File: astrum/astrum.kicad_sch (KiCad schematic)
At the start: 17 parts, among them J1 USB_C_Receptacle_USB2.0_16P, J2 Micro_SD_Card, U1 STM32H523CEUx, U3 USBLC6-2SC6, U4 W25Q32JVSS, Y1 25 mHz

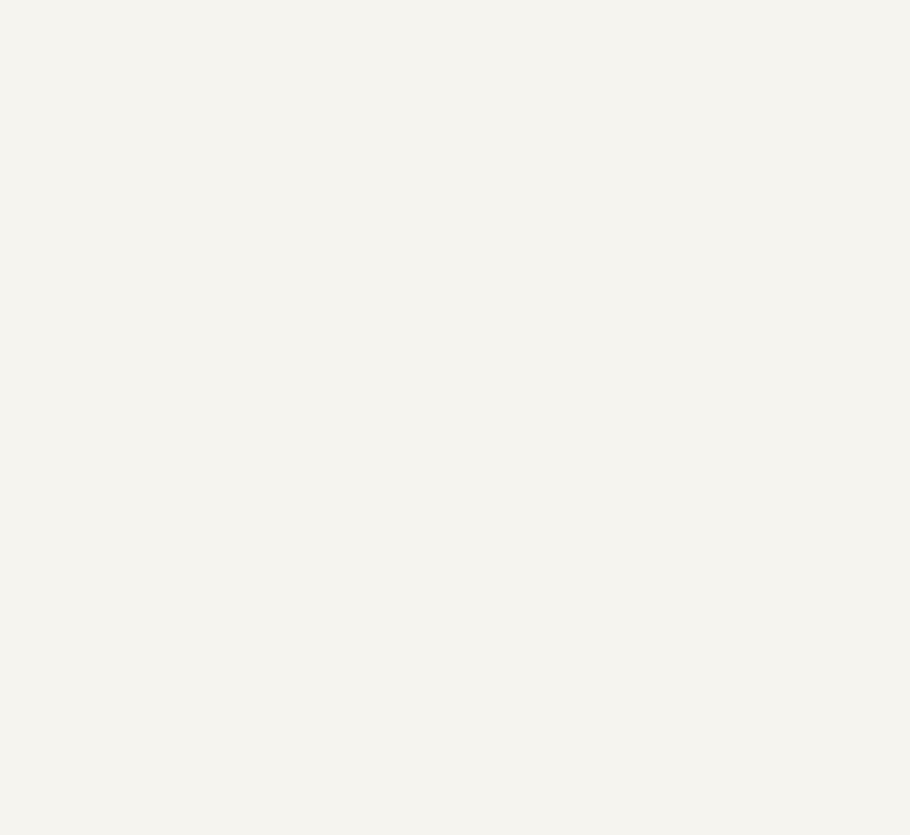
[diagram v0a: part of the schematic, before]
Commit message: add drv8871 drivers to the board
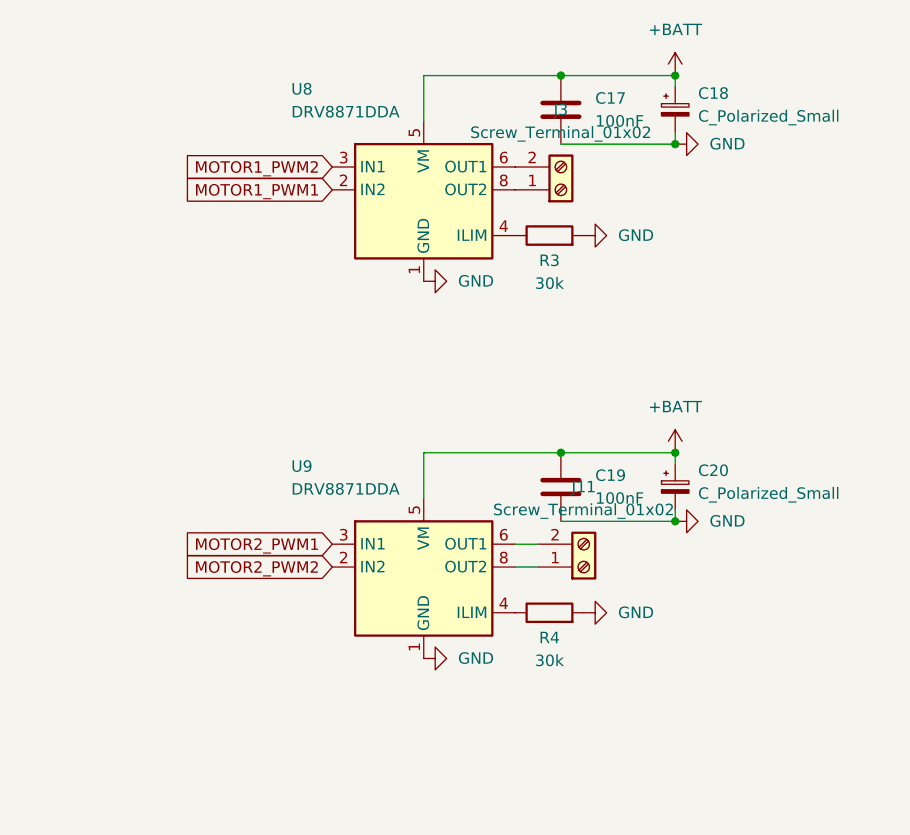
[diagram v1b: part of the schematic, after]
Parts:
- added C17, C19: 100nF, A_HDJ_Library:C_0603_1608Metric, symbol Device:C
- added C18, C20: C_Polarized_Small, Capacitor_SMD:CP_Elec_3x5.3, symbol Device:C_Polarized_Small
- added J11, J3: Screw_Terminal_01x02, TerminalBlock:TerminalBlock_bornier-2_P5.08mm, symbol Connector:Screw_Terminal_01x02
- added R3, R4: 30k, Resistor_SMD:R_0603_1608Metric, symbol Device:R
- added U8, U9: DRV8871DDA, Package_SO:Texas_HTSOP-8-1EP_3.9x4.9mm_P1.27mm_EP2.95x4.9mm_Mask2.4x3.1mm_ThermalVias, symbol Driver_Motor:DRV8871DDA
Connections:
- net GND: now also C17.2, C18.2, C19.2, C20.2, R3.2, R4.2, U8.1 (GND), U8.7 (GND), U8.9 (GND), U9.1 (GND), U9.7 (GND), U9.9 (GND)
- net MOTOR1_PWM1: now also U8.2 (IN2)
- net MOTOR1_PWM2: now also U8.3 (IN1)
- net MOTOR2_PWM1: now also U9.3 (IN1)
- net MOTOR2_PWM2: now also U9.2 (IN2)
- new net: R4.1, U9.4 (ILIM)
- new net: J11.2 (Pin_2), U9.6 (OUT1)
- new net: J11.1 (Pin_1), U9.8 (OUT2)
- new net: R3.1, U8.4 (ILIM)
- new net: J3.2 (Pin_2), U8.6 (OUT1)
- new net: J3.1 (Pin_1), U8.8 (OUT2)
- new net +BATT: C17.1, C18.1, C19.1, C20.1, U8.5 (VM), U9.5 (VM)

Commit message: add imu schematics
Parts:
- added C10: 4.7uF, A_HDJ_Library:C_0603_1608Metric, symbol Device:C
- added C12, C13, C9: 1uF, A_HDJ_Library:C_0603_1608Metric, symbol Device:C
- added C14, C15, C16: 100nF, A_HDJ_Library:C_0603_1608Metric, symbol Device:C
- added D3: NSR0530HT3G, Diode_SMD:D_SOD-323, symbol Device:D_Schottky
- added R5, R7: YC164-JR-0710KL, YC164-JR-0710KL:RESCAXE80P320X160X70-8N, symbol YC164-JR-0710KL:YC164-JR-0710KL
- added U10, U7: BSS138DW-7-F, BSS138DW:SOT363_DIO, symbol 2025-10-04_02-12-38:BSS138DW-7-F
- added U2: LDL212PV33R, LDL212PV33R:SON50P200X200X80-7N, symbol LDL212PV33R:LDL212PV33R
- added U5: ICM-20948, Sensor_Motion:InvenSense_QFN-24_3x3mm_P0.4mm, symbol Sensor_Motion:ICM-20948
- added U6: MIC5317-1.8xM5, Package_TO_SOT_SMD:SOT-23-5, symbol Regulator_Linear:MIC5317-1.8xM5
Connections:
- net +5V: now also D3.2 (A)
- net +BATT: now also C9.1, D3.1 (K), U2.4 (VIN), U2.6 (EN)
- net GND: now also C10.2, C12.2, C13.2, C14.2, C15.2, C16.2, C9.2, U2.1 (GND), U2.7 (GND__1), U5.18 (GND), U5.20 (GND), U6.2 (GND)
- net IMU_INT: now also R5.2, U10.3 (D2)
- net IMU_SCL: now also R7.2, U7.3 (D2)
- net IMU_SDA: now also R7.3, U7.6 (D1)
- net VDD: now also C10.1, C12.1, R5.6, R5.7, R7.6, R7.7, U2.2 (SENSE), U2.3 (VOUT), U6.1 (VIN), U6.3 (EN)
- new net: C14.1, U5.10 (REGOUT)
- new net +1V8: C13.1, C15.1, C16.1, R5.5, R5.8, R7.5, R7.8, U10.2 (G1), U10.5 (G2), U5.13 (VDD), U5.22 (~{CS}), U5.8 (VDDIO), U6.5 (VOUT), U7.2 (G1), U7.5 (G2)
- new net FSYNC_1V8: R5.1, U10.1 (S1), U5.11 (FSYNC)
- new net IMU_FSYNC: R5.3, U10.6 (D1)
- new net INT_1V8: R5.4, U10.4 (S2), U5.12 (INT1)
- new net SCL_1V8: R7.4, U5.23 (SCL/SCLK), U7.4 (S2)
- new net SDA_1V8: R7.1, U5.24 (SDA/SDI), U7.1 (S1)
- no-connect marks 4 -> 6
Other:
- moved on the sheet: C17, C18, C19, C20, J11, J3, R3, R4, U8, U9

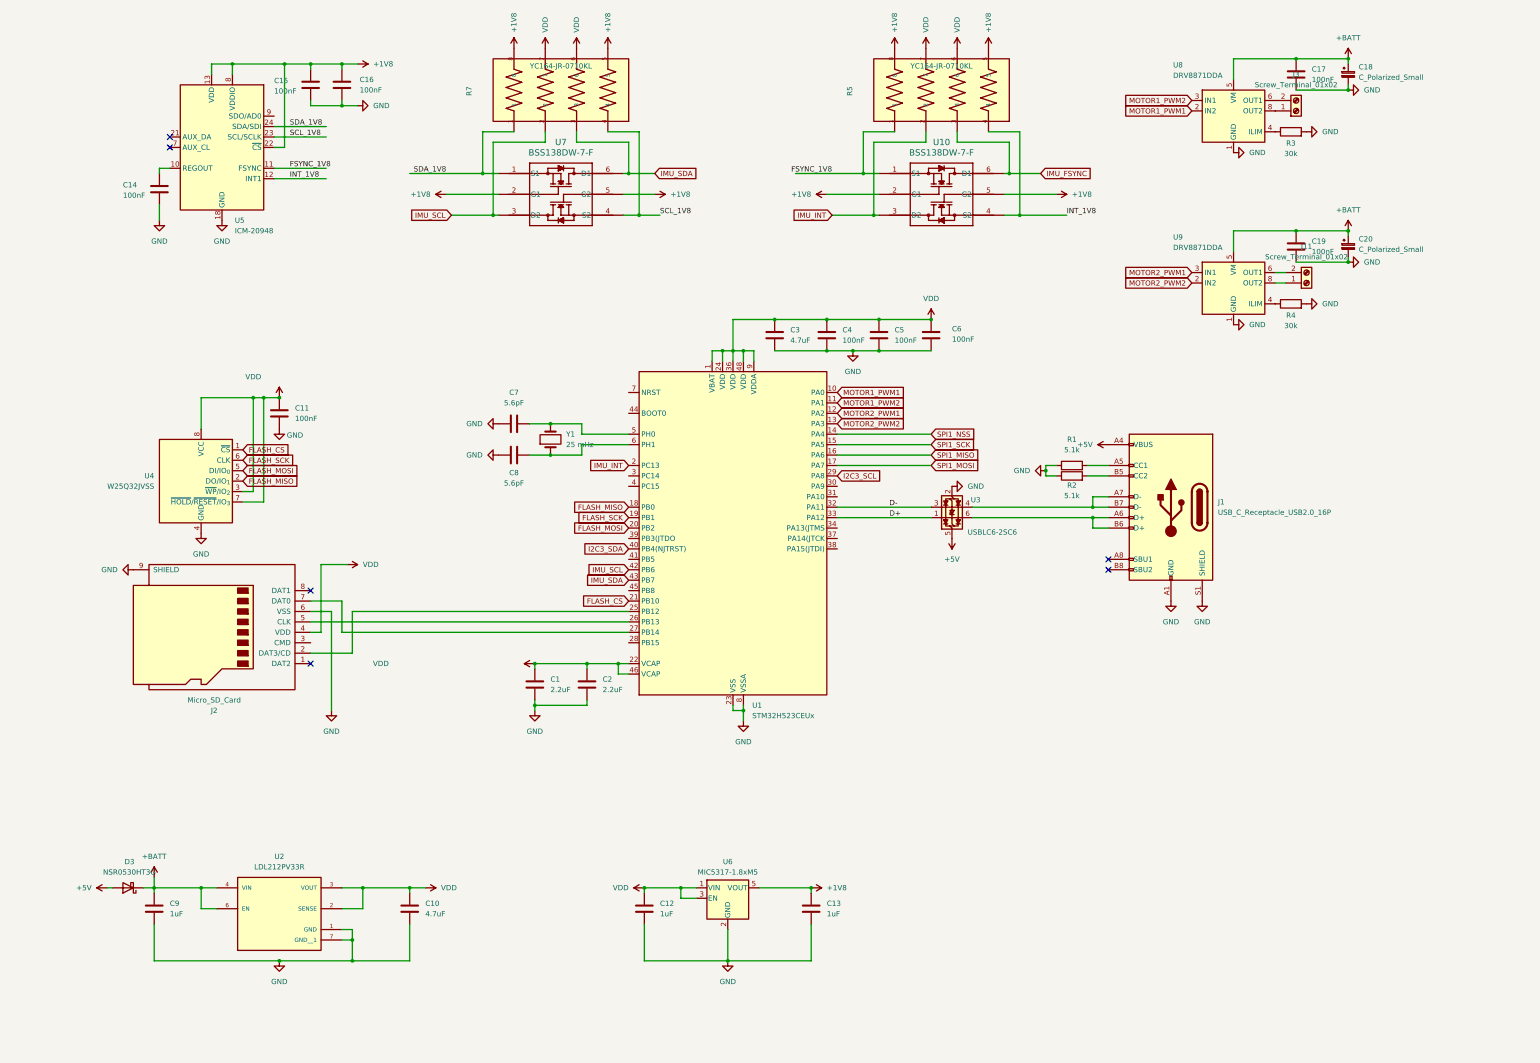
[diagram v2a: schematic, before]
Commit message: add the drv routing and header pins + power supply
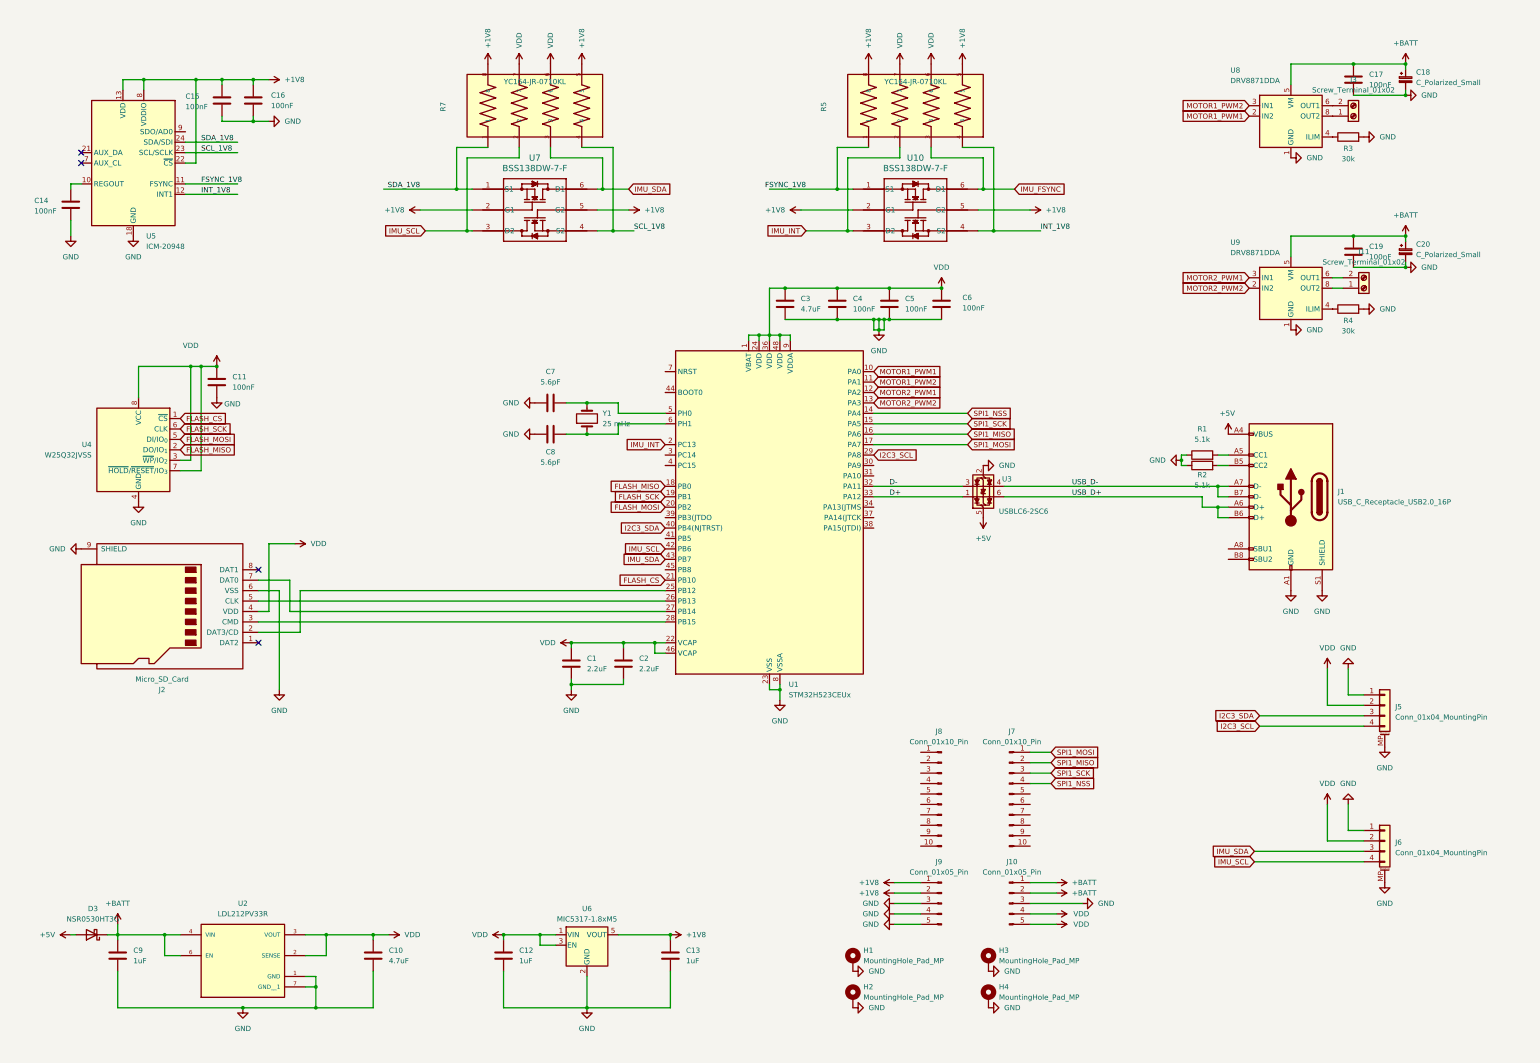
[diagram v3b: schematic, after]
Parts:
- added H1, H2, H3, H4: MountingHole_Pad_MP, MountingHole:MountingHole_2.2mm_M2_ISO7380_Pad, symbol Mechanical:MountingHole_Pad_MP
- added J10, J9: Conn_01x05_Pin, Connector_PinHeader_2.54mm:PinHeader_1x05_P2.54mm_Vertical, symbol Connector:Conn_01x05_Pin
- added J5, J6: Conn_01x04_MountingPin, Connector_JST:JST_SH_SM04B-SRSS-TB_1x04-1MP_P1.00mm_Horizontal, symbol Connector_Generic_MountingPin:Conn_01x04_MountingPin
- added J7, J8: Conn_01x10_Pin, Connector_PinHeader_2.54mm:PinHeader_1x10_P2.54mm_Vertical, symbol Connector:Conn_01x10_Pin
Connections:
- net +1V8: now also J9.1 (Pin_1), J9.2 (Pin_2)
- net +BATT: now also J10.1 (Pin_1), J10.2 (Pin_2)
- net GND: now also H1.MP, H2.MP, H3.MP, H4.MP, J10.3 (Pin_3), J5.1 (Pin_1), J5.MP (MountPin), J6.1 (Pin_1), J6.MP (MountPin), J9.3 (Pin_3), J9.4 (Pin_4), J9.5 (Pin_5)
- net I2C3_SCL: now also J5.4 (Pin_4)
- net I2C3_SDA: now also J5.3 (Pin_3)
- net IMU_SCL: now also J6.4 (Pin_4)
- net IMU_SDA: now also J6.3 (Pin_3)
- net SPI1_MISO: now also J7.2 (Pin_2)
- net SPI1_MOSI: now also J7.1 (Pin_1)
- net SPI1_NSS: now also J7.4 (Pin_4)
- net SPI1_SCK: now also J7.3 (Pin_3)
- net VDD: now also J10.4 (Pin_4), J10.5 (Pin_5), J5.2 (Pin_2), J6.2 (Pin_2)
- net at J2.3 (CMD): now also U1.28 (PB15)
- net USB_D+: now reaches J1.A6 (D+), J1.B6 (D+), U3.6 (I/O1)
- net USB_D-: now reaches J1.A7 (D-), J1.B7 (D-), U3.4 (I/O2)
- no-connect marks 6 -> 4
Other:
- moved on the sheet: C1, C10, C11, C12, C13, C14, C15, C16, C17, C18, C19, C2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

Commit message: add more gpio header things
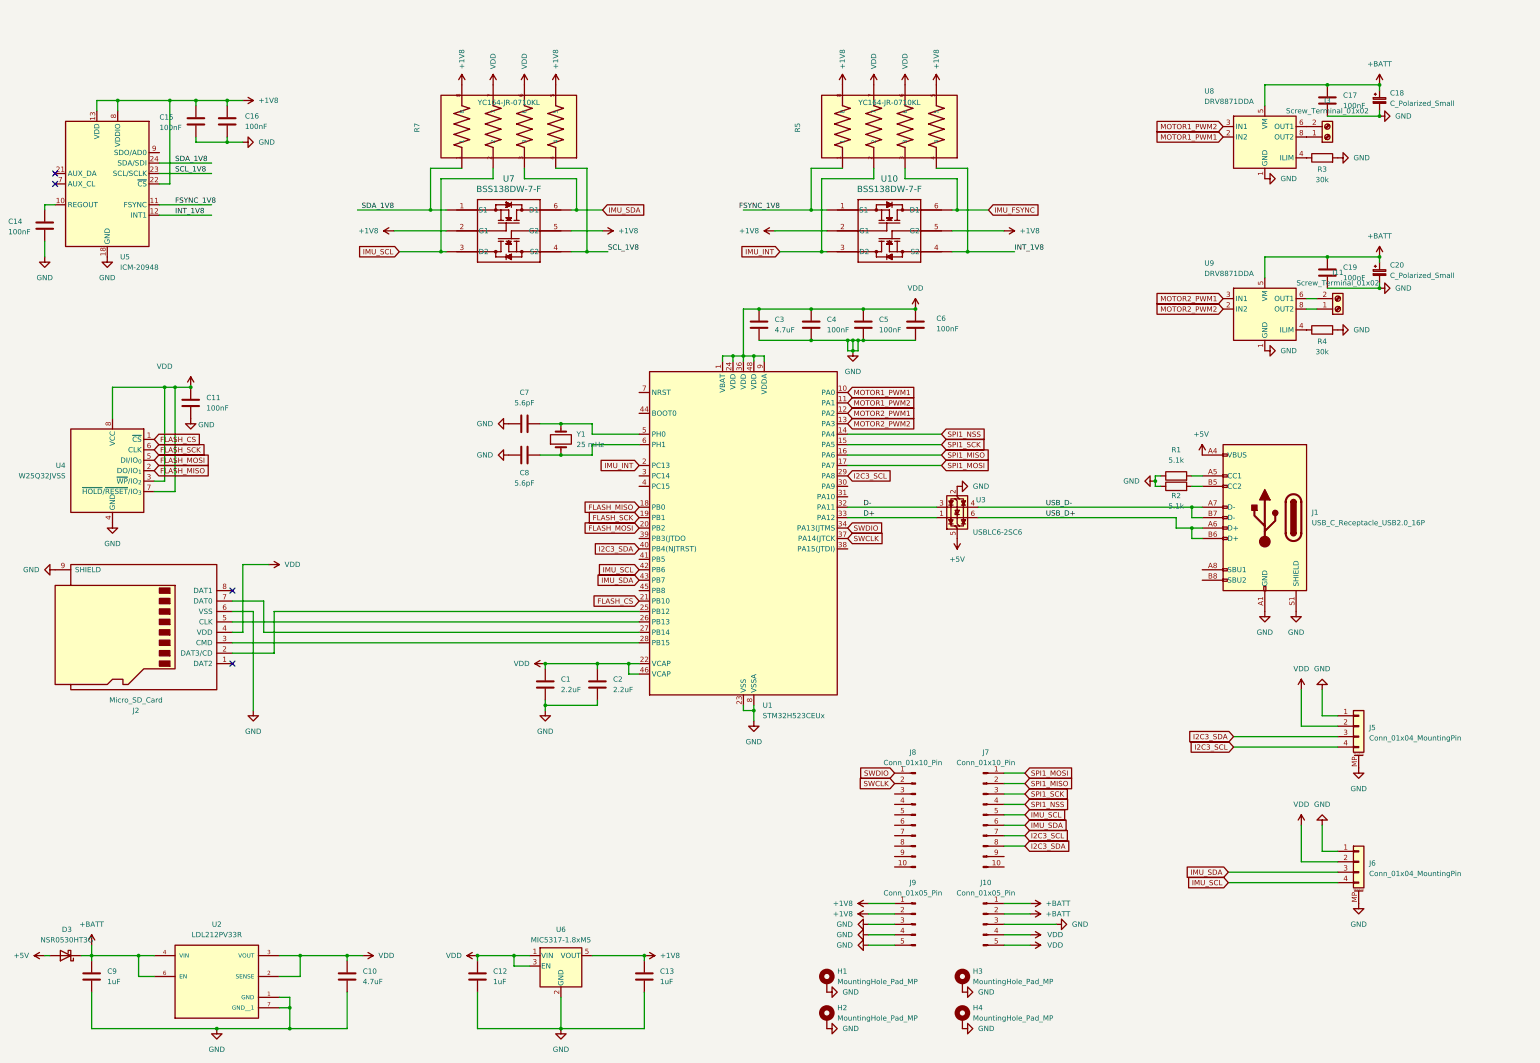
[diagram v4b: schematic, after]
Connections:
- net I2C3_SCL: now also J7.7 (Pin_7)
- net I2C3_SDA: now also J7.8 (Pin_8)
- net IMU_SCL: now also J7.5 (Pin_5)
- net IMU_SDA: now also J7.6 (Pin_6)
- net SWDIO: now reaches J8.1 (Pin_1)
- net SWDIO: now also U1.34 (PA13(JTMS)
- net SWCLK: now reaches J8.2 (Pin_2)
- net SWCLK: now also U1.37 (PA14(JTCK)
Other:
- moved on the sheet: C1, C10, C11, C12, C13, C14, C15, C16, C17, C18, C19, C2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

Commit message: fix the power plane and the mounting holes
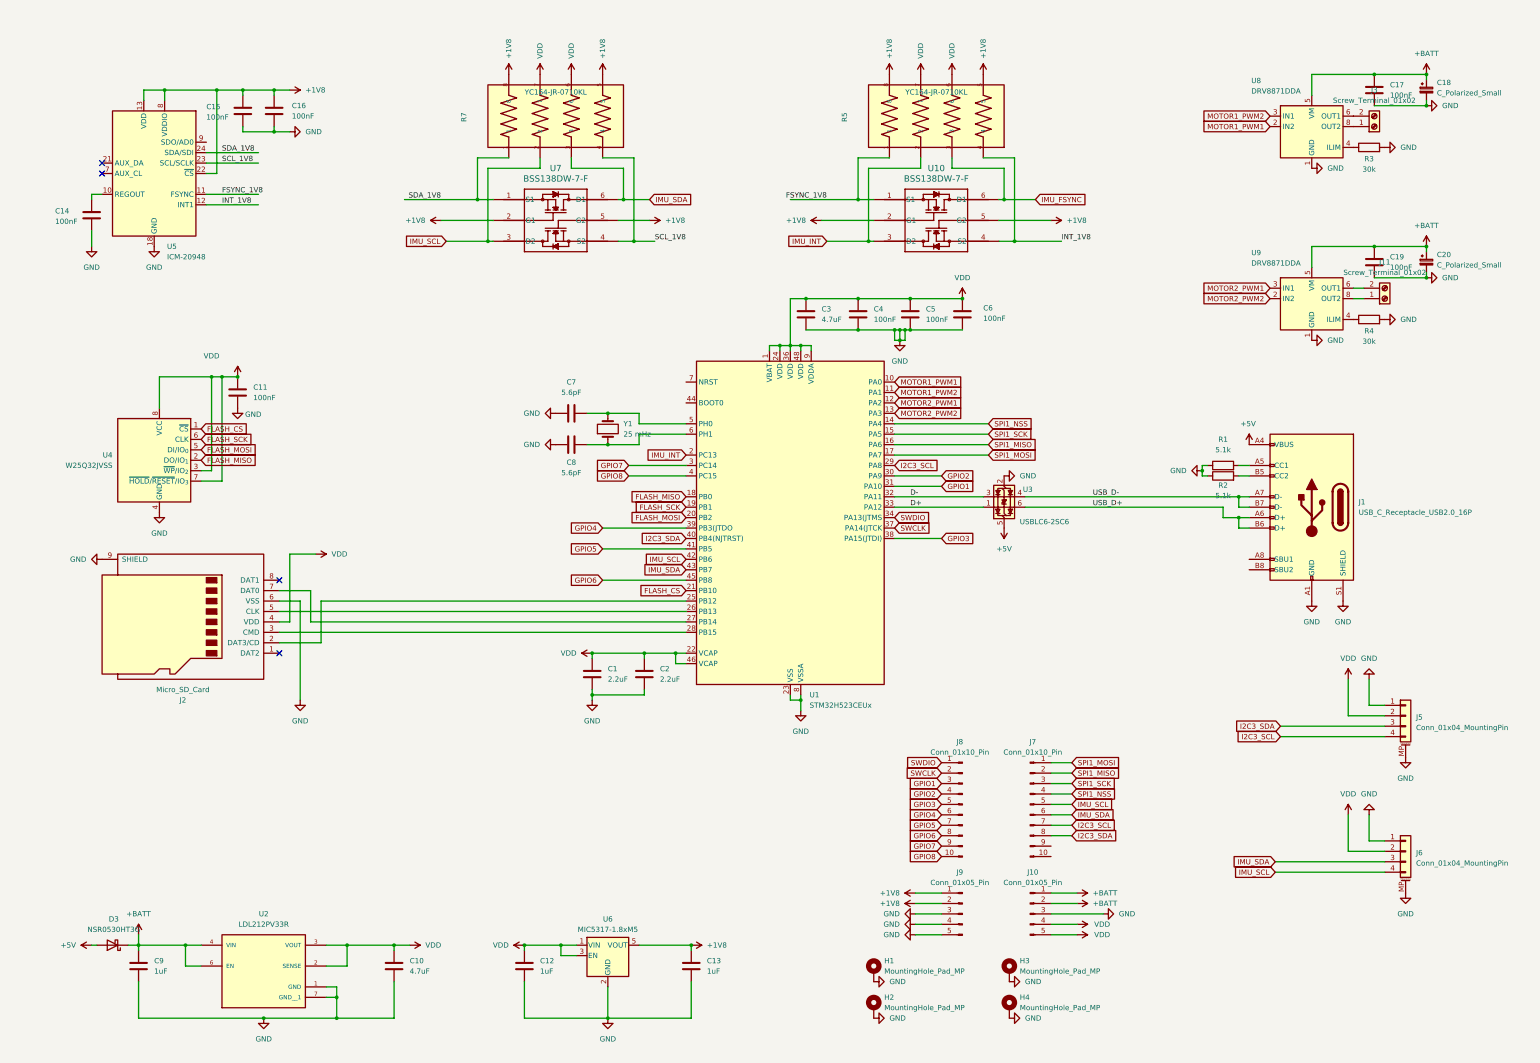
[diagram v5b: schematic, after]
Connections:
- net GPIO8: now reaches J8.10 (Pin_10)
- net GPIO8: now also U1.4 (PC15)
- net GPIO1: now reaches J8.3 (Pin_3)
- net GPIO1: now also U1.31 (PA10)
- net GPIO2: now reaches J8.4 (Pin_4)
- net GPIO2: now also U1.30 (PA9)
- net GPIO3: now reaches J8.5 (Pin_5)
- net GPIO3: now also U1.38 (PA15(JTDI))
- net GPIO4: now reaches J8.6 (Pin_6)
- net GPIO4: now also U1.39 (PB3(JTDO)
- net GPIO5: now reaches J8.7 (Pin_7)
- net GPIO5: now also U1.41 (PB5)
- net GPIO6: now reaches J8.8 (Pin_8)
- net GPIO6: now also U1.45 (PB8)
- net GPIO7: now reaches J8.9 (Pin_9)
- net GPIO7: now also U1.3 (PC14)
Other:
- moved on the sheet: C1, C10, C11, C12, C13, C14, C15, C16, C17, C18, C19, C2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
